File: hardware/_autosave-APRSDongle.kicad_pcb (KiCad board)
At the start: 2 copper layers, 56.6 x 39.2 mm, 34 parts, among them IC1 DRA818, J1 SMA, P1 VIN, P2 GPS, P3 PC_CON, P4 CONN_8, P5 SWD, U1 AP7363, U2 KL05

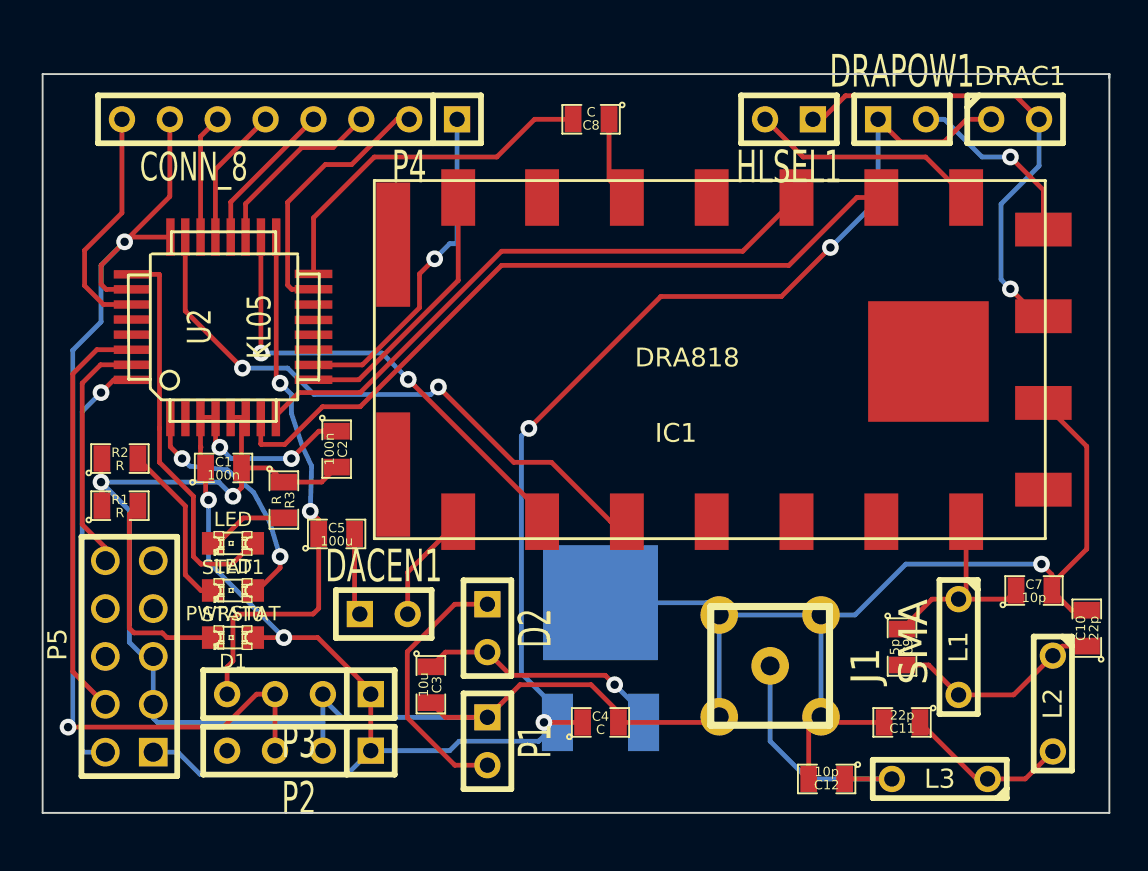
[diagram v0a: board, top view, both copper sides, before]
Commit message: finished routing. Gerber generated.
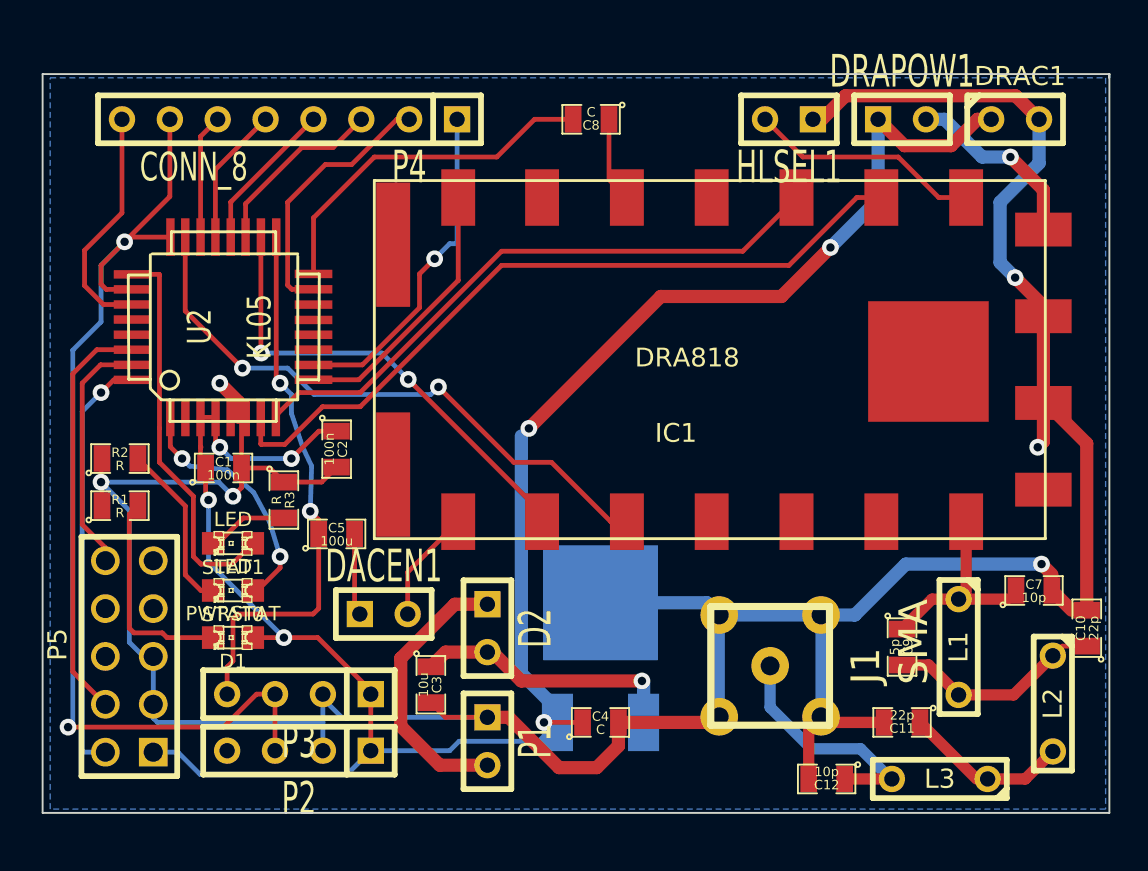
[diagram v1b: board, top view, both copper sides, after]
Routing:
- net GND: track 157.5 -> 168.0 mm, vias 4 -> 6
- net N-0000010: track 13.8 -> 12.7 mm
- net N-000001: track 13.4 -> 14.4 mm
- net N-000007: track 14.1 -> 14.8 mm
- added copper zone on B.Cu, net GND
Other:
- net class RF added: clearance 0.2, trace_width 0.6, via_dia 0.889, via_drill 0.635
- net class power added: clearance 0.175, trace_width 0.7, via_dia 0.889, via_drill 0.635
